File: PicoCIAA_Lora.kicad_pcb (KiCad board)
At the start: 2 copper layers, 47 x 30 mm, 9 parts, among them P1 EDGE_SMA, P3 PWR, P4 MOUNTING_HOLE, P5 MOUNTING_HOLE, P6 IO1, P8 IO3, U1 RFM95

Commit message: PCB: Agregando fiduciales
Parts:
- added REF1: F1, Fiducials:Fiducial_1mm_Dia_2.54mm_Outer_CopperTop, F.Cu at (55.8, 102.7)
- added REF2: F2, Fiducials:Fiducial_1mm_Dia_2.54mm_Outer_CopperTop, F.Cu at (91.6, 124.4)
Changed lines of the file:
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@@
     (links 23)
     (no_connects 8)
-    (area 34.750002 98.6404 149.314286 138.9)
+    (area 52.949999 99.949999 100.050001 130.050001)
     (thickness 1.6)
     (drawings 11)
     (tracks 90)
     (zones 0)
-    (modules 9)
+    (modules 11)
     (nets 34)
   )
@@
       (xy -2.42316 3.59156)) (layer F.SilkS) (width 0.00254))
   )
+  (module Fiducials:Fiducial_1mm_Dia_2.54mm_Outer_CopperTop (layer F.Cu)
+    (at 55.8 102.7)
+    (descr "Circular Fiducial, 1mm bare copper top; 2.54mm keepout")
+    (tags marker)
+    (attr virtual)
+    (fp_text reference REF1 (at -0.1 2.3) (layer F.SilkS)
+      (effects (font (size 1 1) (thickness 0.15)))
+    )
+    (fp_text value F1 (at 0 -1.8) (layer F.Fab)
+      (effects (font (size 1 1) (thickness 0.15)))
+    )
+    (fp_circle (center 0 0) (end 1.55 0) (layer F.CrtYd) (width 0.05))
+    (pad ~ smd circle (at 0 0) (size 1 1) (layers F.Cu F.Mask)
+      (solder_mask_margin 0.77) (clearance 0.77))
+  )
+  (module Fiducials:Fiducial_1mm_Dia_2.54mm_Outer_CopperTop (layer F.Cu)
+    (at 91.6 124.4)
+    (descr "Circular Fiducial, 1mm bare copper top; 2.54mm keepout")
+    (tags marker)
+    (attr virtual)
+    (fp_text reference REF2 (at 0.5 2.4) (layer F.SilkS)
+      (effects (font (size 1 1) (thickness 0.15)))
+    )
+    (fp_text value F2 (at 0 -1.8) (layer F.Fab)
+      (effects (font (size 1 1) (thickness 0.15)))
+    )
+    (fp_circle (center 0 0) (end 1.55 0) (layer F.CrtYd) (width 0.05))
+    (pad ~ smd circle (at 0 0) (size 1 1) (layers F.Cu F.Mask)
+      (solder_mask_margin 0.77) (clearance 0.77))
+  )
   (gr_text "Notas de fabricación\n* Clearance: 0.15mm\n* Ancho de pista: 0.15mm\n* Diámetro vía: 0.70mm\n* Agujero vía: 0.40mm\n\nNro de capas: 2\nEspesor: 1.6mm\nGrilla de posicionamiento: 0.5mm\nGrilla de ruteo: 0.1mm" (at 110.6 114.3) (layer Dwgs.User)

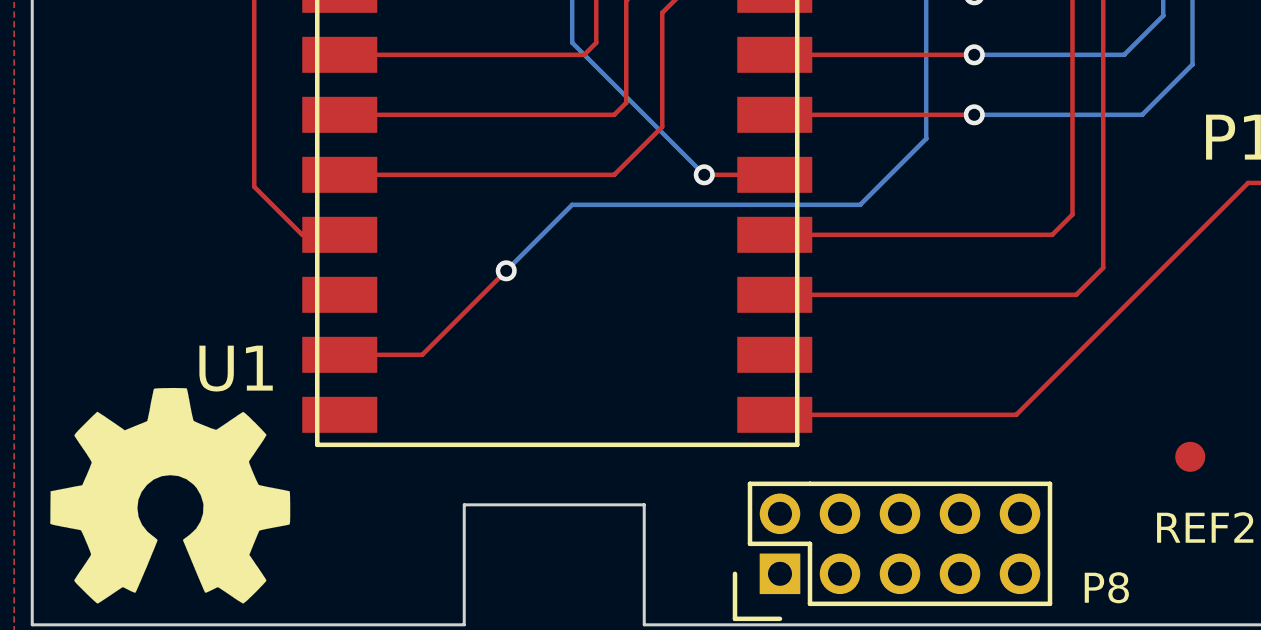
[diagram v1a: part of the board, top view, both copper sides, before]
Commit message: PCB: Acomodando 3D
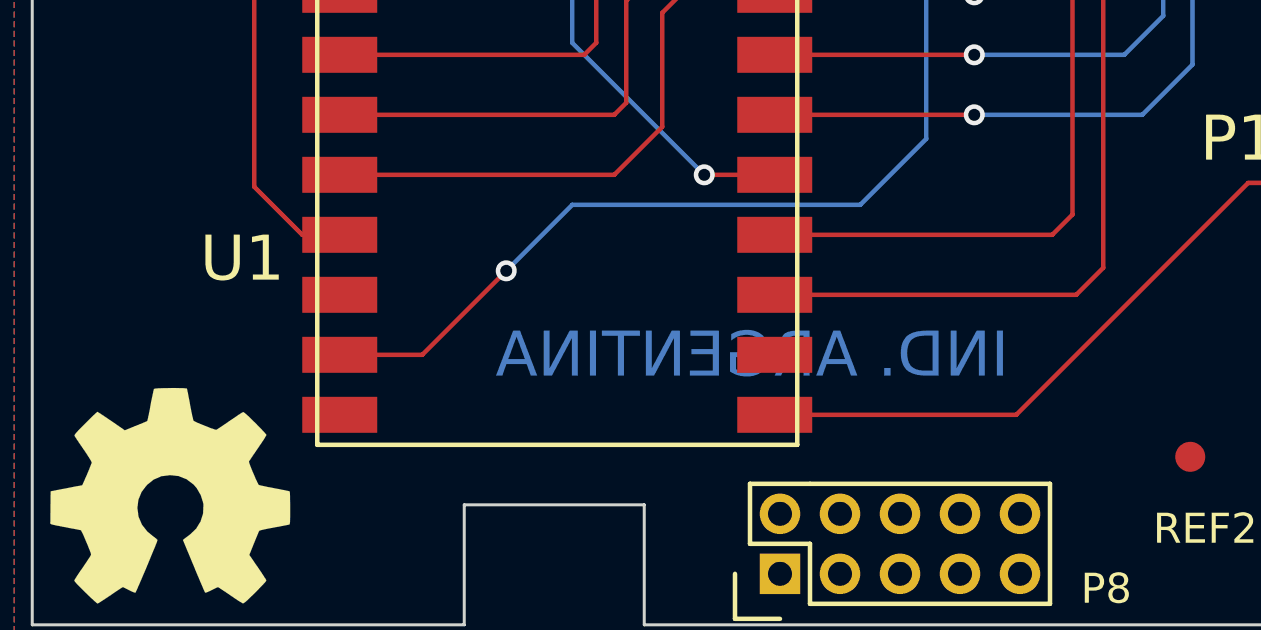
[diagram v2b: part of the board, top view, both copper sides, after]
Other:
- board text added: "IND. ARGENTINA"
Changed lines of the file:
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@@
   (general
     (links 23)
-    (no_connects 8)
+    (no_connects 0)
     (area 52.949999 99.949999 100.050001 130.050001)
     (thickness 1.6)
-    (drawings 11)
+    (drawings 12)
     (tracks 90)
     (zones 0)
@@
   (module footprints:RFM95W (layer F.Cu)
     (at 70.5 116)
-    (fp_text reference U1 (at -10.7 5.5) (layer F.SilkS)
+    (fp_text reference U1 (at -10.5 1.8) (layer F.SilkS)
       (effects (font (size 1.5 1.5) (thickness 0.15)))
     )
-    (fp_text value RFM95 (at -11.9 3) (layer F.Fab)
+    (fp_text value RFM95 (at -11.7 4.3) (layer F.Fab)
       (effects (font (size 1.2 1.2) (thickness 0.15)))
     )
@@
     (pad 1 connect rect (at -9.144 1.27) (size 4.07162 1.99898) (layers F.Cu F.Mask)
       (net 33 "Net-(P1-Pad1)"))
+    (model ${KIPRJMOD}/PicoCIAA_Lora.3dshapes/SMAedge2.wrl
+      (at (xyz -0.16 -0.044 0))
+      (scale (xyz 0.5 0.5 0.5))
+      (rotate (xyz 90 -90 180))
+    )
   )
   (module Capacitors_SMD:C_0805 (layer F.Cu)
@@
     (pad ~ smd circle (at 0 0) (size 1 1) (layers F.Cu F.Mask)
       (solder_mask_margin 0.77) (clearance 0.77))
+  )
+  (gr_text "IND. ARGENTINA" (at 77 121) (layer B.Cu)
+    (effects (font (size 1.5 1.5) (thickness 0.3)) (justify mirror))
   )
   (gr_text "Notas de fabricación\n* Clearance: 0.15mm\n* Ancho de pista: 0.15mm\n* Diámetro vía: 0.70mm\n* Agujero vía: 0.40mm\n\nNro de capas: 2\nEspesor: 1.6mm\nGrilla de posicionamiento: 0.5mm\nGrilla de ruteo: 0.1mm" (at 110.6 114.3) (layer Dwgs.User)
@@
     (connect_pads (clearance 0.508))
     (min_thickness 0.254)
-    (fill (arc_segments 16) (thermal_gap 0.508) (thermal_bridge_width 0.508))
+    (fill yes (arc_segments 16) (thermal_gap 0.508) (thermal_bridge_width 0.508))
     (polygon
       (pts
@@
     (connect_pads (clearance 0.508))
     (min_thickness 0.254)
-    (fill (arc_segments 16) (thermal_gap 0.508) (thermal_bridge_width 0.508))
+    (fill yes (arc_segments 16) (thermal_gap 0.508) (thermal_bridge_width 0.508))
     (polygon
       (pts

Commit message: DRC: Prueba
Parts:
- G101: footprint ej2cese:Logo_OSHWA -> footprints:Logo_OSHWA
- moved G101 0.22 mm to (57.8, 125.6)
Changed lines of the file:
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@@
     )
   )
-  (module ej2cese:Logo_OSHWA (layer F.Cu)
-    (at 57.6 125.7)
-    (fp_text reference G101 (at 0 3.3) (layer F.SilkS) hide
+  (module Fiducials:Fiducial_1mm_Dia_2.54mm_Outer_CopperTop (layer F.Cu)
+    (at 55.8 102.7)
+    (descr "Circular Fiducial, 1mm bare copper top; 2.54mm keepout")
+    (tags marker)
+    (attr virtual)
+    (fp_text reference REF1 (at -0.1 2.3) (layer F.SilkS)
+      (effects (font (size 1 1) (thickness 0.15)))
+    )
+    (fp_text value F1 (at 0 -1.8) (layer F.Fab)
+      (effects (font (size 1 1) (thickness 0.15)))
+    )
+    (fp_circle (center 0 0) (end 1.55 0) (layer F.CrtYd) (width 0.05))
+    (pad ~ smd circle (at 0 0) (size 1 1) (layers F.Cu F.Mask)
+      (solder_mask_margin 0.77) (clearance 0.77))
+  )
+  (module Fiducials:Fiducial_1mm_Dia_2.54mm_Outer_CopperTop (layer F.Cu)
+    (at 91.6 124.4)
+    (descr "Circular Fiducial, 1mm bare copper top; 2.54mm keepout")
+    (tags marker)
+    (attr virtual)
+    (fp_text reference REF2 (at 0.5 2.4) (layer F.SilkS)
+      (effects (font (size 1 1) (thickness 0.15)))
+    )
+    (fp_text value F2 (at 0 -1.8) (layer F.Fab)
+      (effects (font (size 1 1) (thickness 0.15)))
+    )
+    (fp_circle (center 0 0) (end 1.55 0) (layer F.CrtYd) (width 0.05))
+    (pad ~ smd circle (at 0 0) (size 1 1) (layers F.Cu F.Mask)
+      (solder_mask_margin 0.77) (clearance 0.77))
+  )
+  (module footprints:Logo_OSHWA (layer F.Cu)
+    (at 57.8 125.6)
+    (fp_text reference G101 (at 0 3.2) (layer F.SilkS) hide
       (effects (font (size 0.7112 0.4572) (thickness 0.1143)))
     )
-    (fp_text value Logo_OSHWA (at -2.6 -3.6) (layer F.SilkS) hide
+    (fp_text value Logo_OSHWA (at -2.6 -3.4) (layer F.SilkS) hide
       (effects (font (size 0.36322 0.36322) (thickness 0.07112)))
     )
@@
       (xy -2.42316 3.59156)) (layer F.SilkS) (width 0.00254))
   )
-  (module Fiducials:Fiducial_1mm_Dia_2.54mm_Outer_CopperTop (layer F.Cu)
-    (at 55.8 102.7)
-    (descr "Circular Fiducial, 1mm bare copper top; 2.54mm keepout")
-    (tags marker)
-    (attr virtual)
-    (fp_text reference REF1 (at -0.1 2.3) (layer F.SilkS)
-      (effects (font (size 1 1) (thickness 0.15)))
-    )
-    (fp_text value F1 (at 0 -1.8) (layer F.Fab)
-      (effects (font (size 1 1) (thickness 0.15)))
-    )
-    (fp_circle (center 0 0) (end 1.55 0) (layer F.CrtYd) (width 0.05))
-    (pad ~ smd circle (at 0 0) (size 1 1) (layers F.Cu F.Mask)
-      (solder_mask_margin 0.77) (clearance 0.77))
-  )
-  (module Fiducials:Fiducial_1mm_Dia_2.54mm_Outer_CopperTop (layer F.Cu)
-    (at 91.6 124.4)
-    (descr "Circular Fiducial, 1mm bare copper top; 2.54mm keepout")
-    (tags marker)
-    (attr virtual)
-    (fp_text reference REF2 (at 0.5 2.4) (layer F.SilkS)
-      (effects (font (size 1 1) (thickness 0.15)))
-    )
-    (fp_text value F2 (at 0 -1.8) (layer F.Fab)
-      (effects (font (size 1 1) (thickness 0.15)))
-    )
-    (fp_circle (center 0 0) (end 1.55 0) (layer F.CrtYd) (width 0.05))
-    (pad ~ smd circle (at 0 0) (size 1 1) (layers F.Cu F.Mask)
-      (solder_mask_margin 0.77) (clearance 0.77))
-  )
   (gr_text "IND. ARGENTINA" (at 77 121) (layer B.Cu)
